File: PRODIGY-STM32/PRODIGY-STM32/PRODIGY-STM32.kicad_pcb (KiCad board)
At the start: 2 copper layers, 55 x 40 mm, 64 parts, among them J1 DF40C-100DP-04V-51, J2 DF40C-100DP-04V-51, Q1 BC850, U1 AP2112K-3.3, U2 STM32F103C8Tx, U3 STM32F407VGTx, Y1 8MHz, Y2 8MHz, Y3 32.768kHz

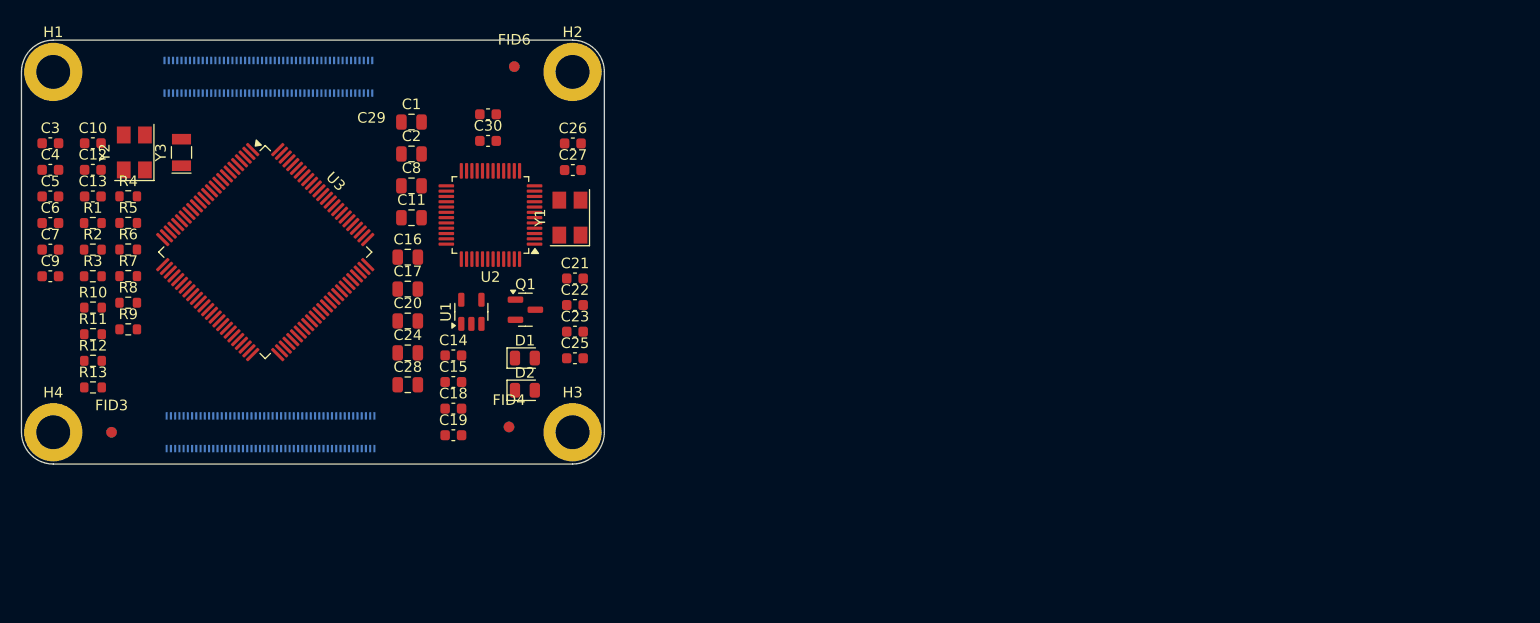
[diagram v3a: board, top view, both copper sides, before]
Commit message: stm32 started, footprints updated, lazout started
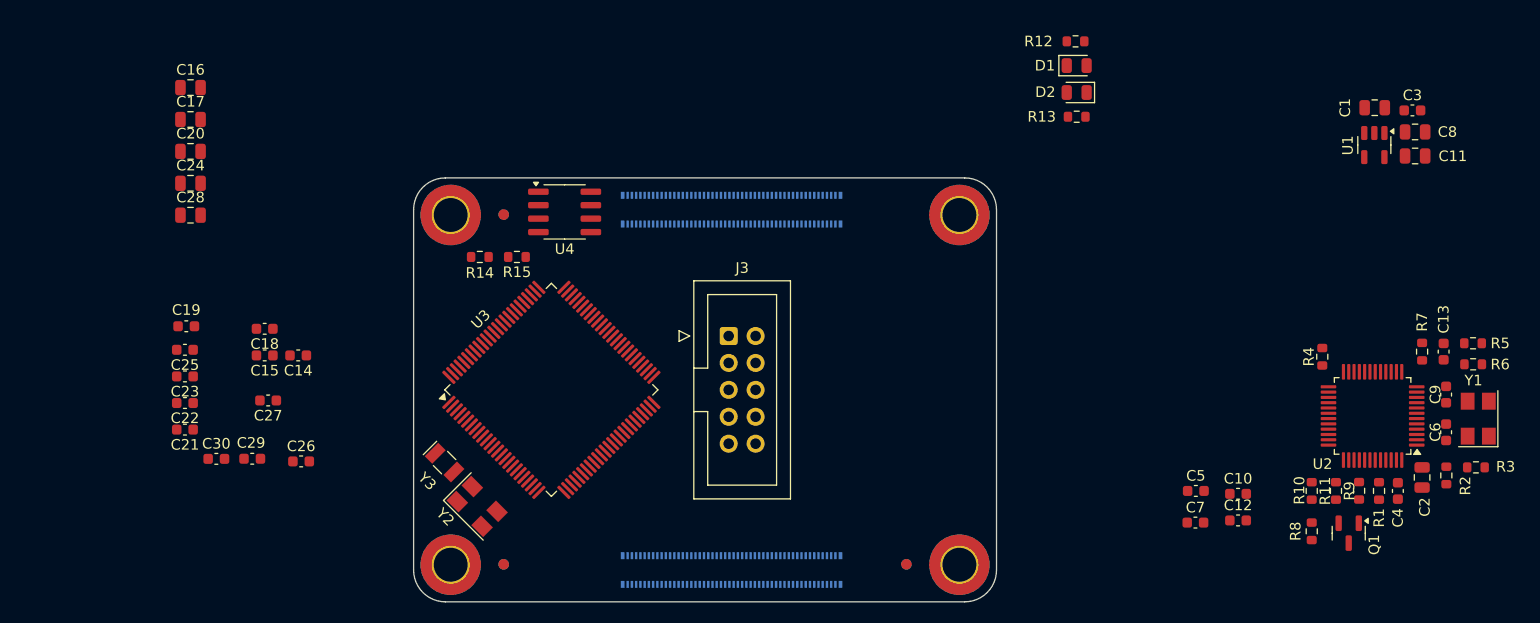
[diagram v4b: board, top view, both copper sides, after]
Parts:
- added J3: Conn_ARM_JTAG_SWD_10, Connector_IDC:IDC-Header_2x05_P2.54mm_Vertical, F.Cu at (166.7, 82.9)
- added R14: DNP, Resistor_SMD:R_0603_1608Metric, F.Cu at (143.2, 75.5)
- added R15: DNP, Resistor_SMD:R_0603_1608Metric, F.Cu at (146.8, 75.5)
- added U4: M24C32-WMN6TP, Package_SO:SOIC-8_3.9x4.9mm_P1.27mm, F.Cu at (151.2, 71.2)
- H1, H2, H3, H4: footprint MountingHole:MountingHole_3.2mm_M3_ISO14580_Pad -> MountingHole:MountingHole_3.2mm_M3_ISO7380_Pad_TopBottom
- J1, J2: footprint DF40C:HIROSE_DF40C-100DS-0.4V_51_ -> DF40C-100DP-0:DF40C100DP04V51
- moved C6 133.2 mm to (234.4, 92.0), turned to -90 degrees
- moved C9 132.2 mm to (234.4, 88.4), turned to 90 degrees
- moved R3 131.7 mm to (237.2, 95.3)
- moved C4 130.7 mm to (229.9, 97.5), turned to -90 degrees
- moved R2 129.5 mm to (234.4, 96.1), turned to -90 degrees
- moved C3 128.6 mm to (231.2, 61.6)
- moved C13 128.3 mm to (234.2, 84.4), turned to 90 degrees
- moved R5 127.4 mm to (237.0, 83.6), turned to 180 degrees
- moved R6 127.4 mm to (237.0, 85.6)
- moved R1 124.0 mm to (228.1, 97.5), turned to -90 degrees
- moved R7 122.3 mm to (232.2, 84.4), turned to -90 degrees
- moved R11 118.2 mm to (224.0, 97.5), turned to 90 degrees
- moved R9 117.1 mm to (226.2, 97.5), turned to -90 degrees
- moved R10 116.3 mm to (221.7, 97.5), turned to 90 degrees
- moved R8 113.7 mm to (221.7, 101.3), turned to -90 degrees
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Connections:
- net /mcu/T_DIO renamed /st-link-v2/T_DIO
- net /mcu/T_RST renamed /st-link-v2/T_RST
- net /mcu/T_SWO renamed /st-link-v2/T_SWO
- J1 pad 1: /Connector-1/USB_HOST_FAULT -> /Connector-1/ANALOG_MICROPHONE
- J1 pad 10: /Connector-1/SERIAL_OUT_TX2 -> GND
- J1 pad 100: /Connector-1/ANALOG_BREAKOUT_PIEZO -> /Connector-1/USB_HOST_ENABLE
- J1 pad 11: /Connector-1/SERIAL_OUT_TX1 -> unconnected-(J1-Pad11)
- J1 pad 12: /Connector-1/SERIAL_OUT_RX2 -> unconnected-(J1-Pad12)
- J1 pad 13: GND -> /Connector-1/ANALOG_JOYSTICK_X
- J1 pad 14: GND -> /Connector-1/ANALOG_HEATER_TEMPERATURE
- J1 pad 15: /Connector-1/CAN_OUT_TX1 -> GND
- J1 pad 16: /Connector-1/CAN_EN -> GND
- J1 pad 17: /Connector-1/CAN_OUT_RX1 -> unconnected-(J1-Pad17)
- J1 pad 18: /Connector-1/CAN_SILENT -> unconnected-(J1-Pad18)
- J1 pad 19: GND -> /Connector-1/ANALOG_PHOTOTRANSISTOR
- J1 pad 2: /Connector-1/USB_HOST_ENABLE -> /Connector-1/ANALOG_BREAKOUT_PIEZO
- J1 pad 20: GND -> /Connector-1/ANALOG_POTENTIOMETER
- J1 pad 21: /Connector-1/I2C_SDA -> GND
- J1 pad 22: /Connector-1/SPI_MOSI -> GND
- J1 pad 23: /Connector-1/I2C_SCL -> unconnected-(J1-Pad23)
- J1 pad 24: /Connector-1/SPI_MISO -> unconnected-(J1-Pad24)
- J1 pad 25: GND -> unconnected-(J1-Pad25)
- J1 pad 26: GND -> unconnected-(J1-Pad26)
- J1 pad 27: /Connector-1/I2C_INTERRUPT_ACCEL -> GND
- J1 pad 28: /Connector-1/SPI_SCK -> GND
- J1 pad 29: /Connector-1/I2C_INTERRUPT_KEYPAD -> unconnected-(J1-Pad29)
- J1 pad 3: /Connector-1/USB_DP- -> GND
- J1 pad 30: /Connector-1/SPI_CS_BREAKOUT -> unconnected-(J1-Pad30)
- J1 pad 31: GND -> unconnected-(J1-Pad31)
- J1 pad 32: GND -> unconnected-(J1-Pad32)
- J1 pad 33: /Connector-1/DIGITAL_IR_EMITTER -> GND
- J1 pad 34: /Connector-1/SPI_CS_SEVENSEG -> GND
- J1 pad 35: /Connector-1/DIGITAL_IR_RECEIVER -> /Connector-1/MOTOR_CC_IN_1
- J1 pad 36: /Connector-1/SPI_CS_TFT -> /Connector-1/MOTOR_CC_IN_2
- J1 pad 37: GND -> /Connector-1/MOTOR_PWM_OUT_1
- J1 pad 38: GND -> /Connector-1/MOTOR_PWM_OUT_2
- J1 pad 39: /Connector-1/DIGITAL_NEOPIXEL_OUT -> GND
- J1 pad 4: /Connector-1/USB_HOST_OUT_P- -> GND
- J1 pad 40: /Connector-1/SPI_TFT_DC -> GND
- J1 pad 41: /Connector-1/DIGITAL_RGB_R -> /Connector-1/DIGITAL_LED_OUT_1
- J1 pad 42: /Connector-1/SPI_TFT_RESET -> /Connector-1/DIGITAL_BUZZER_OUT
- J1 pad 43: /Connector-1/DIGITAL_RGB_G -> /Connector-1/DIGITAL_LED_OUT_0
- J1 pad 44: GND -> /Connector-1/DIGITAL_LED_OUT_2
- J1 pad 45: /Connector-1/DIGITAL_RGB_B -> GND
- J1 pad 46: /Connector-1/SPI_CS_NFC -> GND
- J1 pad 47: /Connector-1/DIGITAL_BUTTON_IN_0 -> /Connector-1/DIGITAL_BUTTON_IN_3
- J1 pad 48: /Connector-1/SPI_IRQ_NFC -> /Connector-1/DIGITAL_HEATER_OUT
- J1 pad 49: /Connector-1/DIGITAL_BUTTON_IN_1 -> /Connector-1/DIGITAL_BUTTON_IN_2
- J1 pad 5: /st-link-v2/USB_D+ -> unconnected-(J1-Pad5)
- J1 pad 50: GND -> /Connector-1/SPI_RST_NFC
- J1 pad 51: /Connector-1/DIGITAL_BUTTON_IN_2 -> /Connector-1/DIGITAL_BUTTON_IN_1
- J1 pad 52: /Connector-1/SPI_RST_NFC -> GND
- J1 pad 53: /Connector-1/DIGITAL_BUTTON_IN_3 -> /Connector-1/DIGITAL_BUTTON_IN_0
- J1 pad 54: /Connector-1/DIGITAL_HEATER_OUT -> /Connector-1/SPI_IRQ_NFC
- J1 pad 55: GND -> /Connector-1/DIGITAL_RGB_B
- J1 pad 56: GND -> /Connector-1/SPI_CS_NFC
- J1 pad 57: /Connector-1/DIGITAL_LED_OUT_0 -> /Connector-1/DIGITAL_RGB_G
- J1 pad 58: /Connector-1/DIGITAL_LED_OUT_2 -> GND
- J1 pad 59: /Connector-1/DIGITAL_LED_OUT_1 -> /Connector-1/DIGITAL_RGB_R
- J1 pad 6: /Connector-1/USB_HOST_OUT_P+ -> unconnected-(J1-Pad6)
- J1 pad 60: /Connector-1/DIGITAL_BUZZER_OUT -> /Connector-1/SPI_TFT_RESET
- J1 pad 61: GND -> /Connector-1/DIGITAL_NEOPIXEL_OUT
- J1 pad 62: GND -> /Connector-1/SPI_TFT_DC
- J1 pad 63: /Connector-1/MOTOR_PWM_OUT_1 -> GND
- J1 pad 64: /Connector-1/MOTOR_PWM_OUT_2 -> GND
- J1 pad 65: /Connector-1/MOTOR_CC_IN_1 -> /Connector-1/DIGITAL_IR_RECEIVER
- J1 pad 66: /Connector-1/MOTOR_CC_IN_2 -> /Connector-1/SPI_CS_TFT
- J1 pad 67: GND -> /Connector-1/DIGITAL_IR_EMITTER
- J1 pad 68: GND -> /Connector-1/SPI_CS_SEVENSEG
- J1 pad 69: unconnected-(J1-Pad69) -> GND
- J1 pad 7: GND -> /Connector-1/ANALOG_JOYSTICK_Y
- J1 pad 70: unconnected-(J1-Pad70) -> GND
- J1 pad 71: unconnected-(J1-Pad71) -> /Connector-1/I2C_INTERRUPT_KEYPAD
- J1 pad 72: unconnected-(J1-Pad72) -> /Connector-1/SPI_CS_BREAKOUT
- J1 pad 73: GND -> /Connector-1/I2C_INTERRUPT_ACCEL
- J1 pad 74: GND -> /Connector-1/SPI_SCK
- J1 pad 75: unconnected-(J1-Pad75) -> GND
- J1 pad 76: unconnected-(J1-Pad76) -> GND
- J1 pad 77: unconnected-(J1-Pad77) -> /mcu/SCL
- J1 pad 78: unconnected-(J1-Pad78) -> /Connector-1/SPI_MISO
- J1 pad 79: GND -> /mcu/SDA
- J1 pad 8: GND -> /Connector-1/ANALOG_BREAKOUT_PT100
- J1 pad 80: GND -> /Connector-1/SPI_MOSI
- J1 pad 81: /Connector-1/ANALOG_PHOTOTRANSISTOR -> GND
- J1 pad 82: /Connector-1/ANALOG_POTENTIOMETER -> GND
- J1 pad 83: unconnected-(J1-Pad83) -> /Connector-1/CAN_OUT_RX1
- J1 pad 84: unconnected-(J1-Pad84) -> /Connector-1/CAN_SILENT
- J1 pad 85: GND -> /Connector-1/CAN_OUT_TX1
- J1 pad 86: GND -> /Connector-1/CAN_EN
- J1 pad 87: /Connector-1/ANALOG_JOYSTICK_X -> GND
- J1 pad 88: /Connector-1/ANALOG_HEATER_TEMPERATURE -> GND
- J1 pad 89: unconnected-(J1-Pad89) -> /Connector-1/SERIAL_OUT_TX1
- J1 pad 9: /Connector-1/SERIAL_OUT_RX1 -> GND
- J1 pad 90: unconnected-(J1-Pad90) -> /Connector-1/SERIAL_OUT_RX2
- J1 pad 91: GND -> /Connector-1/SERIAL_OUT_RX1
- J1 pad 92: GND -> /Connector-1/SERIAL_OUT_TX2
- J1 pad 93: /Connector-1/ANALOG_JOYSTICK_Y -> GND
- J1 pad 94: /Connector-1/ANALOG_BREAKOUT_PT100 -> GND
- J1 pad 95: unconnected-(J1-Pad95) -> /st-link-v2/USB_D+
- J1 pad 96: unconnected-(J1-Pad96) -> /Connector-1/USB_HOST_OUT_P+
- J1 pad 97: GND -> /Connector-1/USB_DP-
- J1 pad 98: GND -> /Connector-1/USB_HOST_OUT_P-
- J1 pad 99: /Connector-1/ANALOG_MICROPHONE -> /Connector-1/USB_HOST_FAULT
- J2 pad 1: GND -> unconnected-(J2-Pad1)
- J2 pad 100: /Connector-2/MCU_RESET -> GND
- J2 pad 12: unconnected-(J2-Pad12) -> +3V3
- J2 pad 13: GND -> +5V
- J2 pad 14: GND -> +3V3
- J2 pad 15: unconnected-(J2-Pad15) -> +5V
- J2 pad 16: unconnected-(J2-Pad16) -> +3V3
- J2 pad 17: unconnected-(J2-Pad17) -> +5V
- J2 pad 18: unconnected-(J2-Pad18) -> +3V3
- J2 pad 19: unconnected-(J2-Pad19) -> +5V
- J2 pad 2: GND -> /Connector-2/MCU_RESET
- J2 pad 21: unconnected-(J2-Pad21) -> +5V
- J2 pad 22: GND -> unconnected-(J2-Pad22)
- J2 pad 23: GND -> +5V
- J2 pad 24: /Connector-2/MCU_GPIO_26 -> /Connector-2/MCU_VREF
- J2 pad 25: /Connector-2/MCU_GPIO_21 -> /Connector-2/SD_Enable
- J2 pad 26: /Connector-2/MCU_GPIO_19 -> /Connector-2/SD_DET
- J2 pad 27: /Connector-2/MCU_GPIO_20 -> unconnected-(J2-Pad27)
- J2 pad 28: /Connector-2/MCU_GPIO_13 -> GND
- J2 pad 29: /Connector-2/MCU_GPIO_16 -> GND
- J2 pad 30: /Connector-2/MCU_GPIO_6 -> unconnected-(J2-Pad30)
- J2 pad 31: /Connector-2/MCU_GPIO_12 -> /Connector-2/SD_DAT2
- J2 pad 32: GND -> unconnected-(J2-Pad32)
- J2 pad 33: GND -> /Connector-2/SD_DAT1
- J2 pad 34: /Connector-2/MCU_GPIO_5 -> unconnected-(J2-Pad34)
- J2 pad 35: unconnected-(J2-Pad35) -> GND
- J2 pad 36: unconnected-(J2-Pad36) -> GND
- J2 pad 37: /Connector-2/MCU_GPIO_7 -> /Connector-2/SD_DAT0
- J2 pad 38: /Connector-2/MCU_GPIO_11 -> unconnected-(J2-Pad38)
- J2 pad 39: /Connector-2/MCU_GPIO_8 -> /Connector-2/SD_DAT3
- J2 pad 4: unconnected-(J2-Pad4) -> GND
- J2 pad 40: /Connector-2/MCU_GPIO_9 -> /Connector-2/SD_CMD
- J2 pad 41: /Connector-2/MCU_GPIO_25 -> GND
- J2 pad 43: GND -> /Connector-2/SD_CLK
- J2 pad 44: /Connector-2/MCU_GPIO_10 -> /Connector-2/MCU_GPIO_2
- J2 pad 45: /Connector-2/MCU_GPIO_24 -> /Connector-2/MCU_GPIO_14
- J2 pad 46: /Connector-2/MCU_GPIO_22 -> /Connector-2/MCU_GPIO_3
- J2 pad 47: /Connector-2/MCU_GPIO_23 -> GND
- J2 pad 48: /Connector-2/MCU_GPIO_27 -> /Connector-2/MCU_GPIO_4
- J2 pad 49: /Connector-2/MCU_GPIO_18 -> /Connector-2/MCU_GPIO_15
- J2 pad 50: /Connector-2/MCU_GPIO_17 -> GND
- J2 pad 51: /Connector-2/MCU_GPIO_15 -> /Connector-2/MCU_GPIO_18
- J2 pad 52: GND -> /Connector-2/MCU_GPIO_17
- J2 pad 53: GND -> /Connector-2/MCU_GPIO_23
- J2 pad 54: /Connector-2/MCU_GPIO_4 -> /Connector-2/MCU_GPIO_27
- J2 pad 55: /Connector-2/MCU_GPIO_14 -> /Connector-2/MCU_GPIO_24
- J2 pad 56: /Connector-2/MCU_GPIO_3 -> /Connector-2/MCU_GPIO_22
- J2 pad 57: /Connector-2/SD_CLK -> GND
- J2 pad 58: /Connector-2/MCU_GPIO_2 -> /Connector-2/MCU_GPIO_10
- J2 pad 59: GND -> /Connector-2/MCU_GPIO_25
- J2 pad 61: /Connector-2/SD_DAT3 -> /Connector-2/MCU_GPIO_8
- J2 pad 62: /Connector-2/SD_CMD -> /Connector-2/MCU_GPIO_9
- J2 pad 63: /Connector-2/SD_DAT0 -> /Connector-2/MCU_GPIO_7
- J2 pad 64: unconnected-(J2-Pad64) -> /Connector-2/MCU_GPIO_11
- J2 pad 65: GND -> unconnected-(J2-Pad65)
- J2 pad 66: GND -> unconnected-(J2-Pad66)
- J2 pad 67: /Connector-2/SD_DAT1 -> GND
- J2 pad 68: unconnected-(J2-Pad68) -> /Connector-2/MCU_GPIO_5
- J2 pad 69: /Connector-2/SD_DAT2 -> /Connector-2/MCU_GPIO_12
- J2 pad 7: GND -> unconnected-(J2-Pad7)
- J2 pad 70: unconnected-(J2-Pad70) -> GND
- J2 pad 71: GND -> /Connector-2/MCU_GPIO_16
- J2 pad 72: unconnected-(J2-Pad72) -> /Connector-2/MCU_GPIO_6
- J2 pad 73: unconnected-(J2-Pad73) -> /Connector-2/MCU_GPIO_20
- J2 pad 74: GND -> /Connector-2/MCU_GPIO_13
- J2 pad 75: /Connector-2/SD_Enable -> /Connector-2/MCU_GPIO_21
- J2 pad 76: /Connector-2/SD_DET -> /Connector-2/MCU_GPIO_19
- J2 pad 77: +5V -> GND
- J2 pad 78: /Connector-2/MCU_VREF -> /Connector-2/MCU_GPIO_26
- J2 pad 79: +5V -> unconnected-(J2-Pad79)
- J2 pad 8: GND -> unconnected-(J2-Pad8)
- J2 pad 80: unconnected-(J2-Pad80) -> GND
- J2 pad 81: +5V -> unconnected-(J2-Pad81)
- J2 pad 83: +5V -> unconnected-(J2-Pad83)
- J2 pad 84: +3V3 -> unconnected-(J2-Pad84)
- J2 pad 85: +5V -> unconnected-(J2-Pad85)
- J2 pad 86: +3V3 -> unconnected-(J2-Pad86)
- J2 pad 87: +5V -> GND
- J2 pad 88: +3V3 -> GND
- J2 pad 90: +3V3 -> unconnected-(J2-Pad90)
- J2 pad 93: unconnected-(J2-Pad93) -> GND
- J2 pad 94: unconnected-(J2-Pad94) -> GND
- J2 pad 98: GND -> unconnected-(J2-Pad98)
- J2 pad 99: unconnected-(J2-Pad99) -> GND
- U3 pad 92: /Connector-1/I2C_SCL -> /mcu/SCL
- U3 pad 93: /Connector-1/I2C_SDA -> /mcu/SDA
- Y1 pad 2: Net-(U2-PD1) -> GND
- Y1 pad 3: (no net) -> Net-(U2-PD1)
- Y1 pad 4: (no net) -> GND
- Y2 pad 2: Net-(U3-PH1) -> GND
- Y2 pad 3: (no net) -> Net-(U3-PH1)
- Y2 pad 4: (no net) -> GND
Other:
- copper layers 2 -> 4

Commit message: stm32 layout done, schematic swd coinnector updated
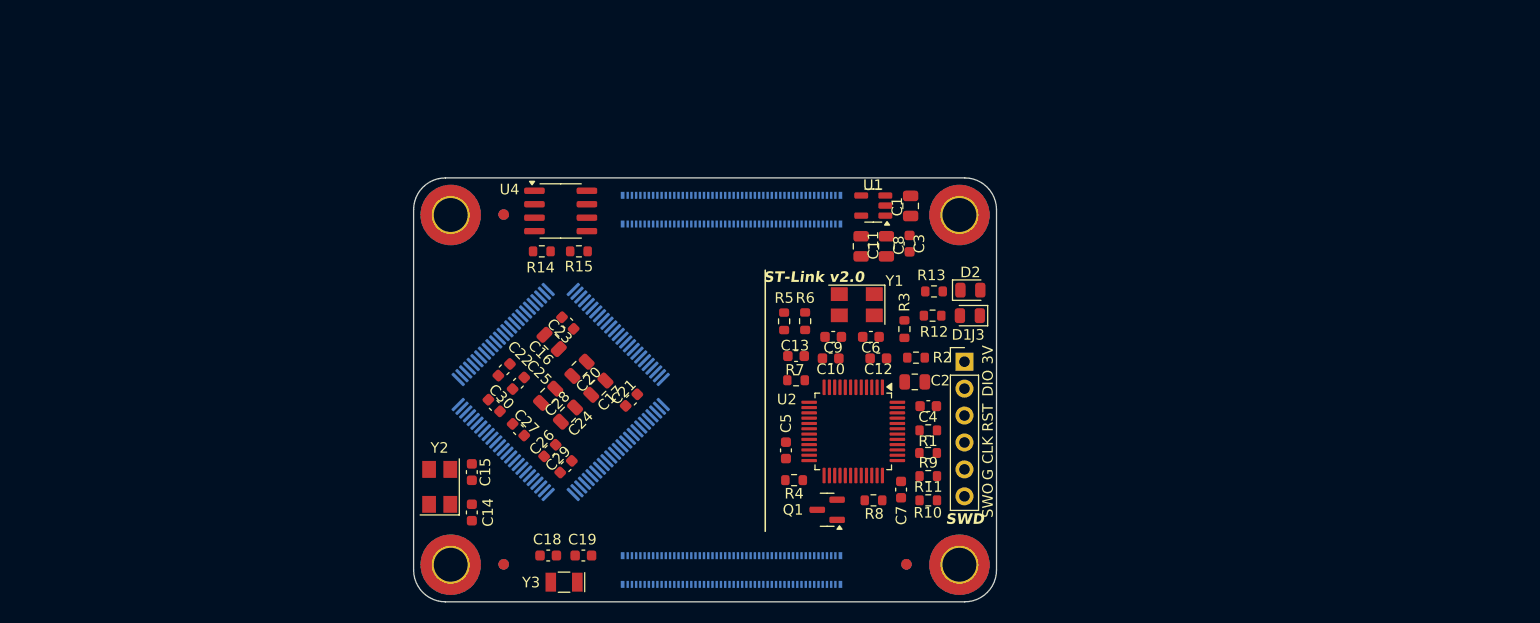
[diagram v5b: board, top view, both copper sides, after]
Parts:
- J3: value Conn_ARM_JTAG_SWD_10 -> Conn_ARM_SWD_TagConnect_TC2030; footprint Connector_IDC:IDC-Header_2x05_P2.54mm_Vertical -> Connector_PinHeader_2.54mm:PinHeader_1x06_P2.54mm_Vertical
- U3: moved to B.Cu
- moved R5 65.0 mm to (172.0, 81.5), turned to -90 degrees
- moved R6 63.2 mm to (173.9, 81.5), turned to 90 degrees
- moved C13 61.1 mm to (173.1, 84.8), turned to 180 degrees
- moved Y1 59.6 mm to (178.8, 80.0), turned to 180 degrees
- moved R7 59.1 mm to (173.1, 87.1), turned to 0 degrees
- moved C9 58.1 mm to (176.6, 83.0), turned to 180 degrees
- moved R3 55.5 mm to (183.3, 82.3), turned to 90 degrees
- moved C6 55.0 mm to (180.2, 83.0), turned to 0 degrees
- moved C11 53.0 mm to (179.2, 74.5), turned to -90 degrees
- moved R2 51.3 mm to (184.4, 85.0), turned to 0 degrees
- moved R4 51.2 mm to (172.9, 96.5), turned to 0 degrees
- moved C8 51.0 mm to (181.6, 74.5), turned to -90 degrees
- moved Q1 49.3 mm to (176.0, 99.3), turned to 180 degrees
- moved C3 49.1 mm to (183.8, 74.2), turned to -90 degrees
- moved U2 49.0 mm to (178.5, 91.9), turned to -90 degrees
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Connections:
- J3 pad 3: GND -> /st-link-v2/T_RST
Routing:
- added copper zone on In2.Cu, net GND
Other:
- board text added: "3V"
- board text added: "CLK"
- board text added: "DIO"
- board text added: "G"
- board text added: "RST"
- board text added: "ST-Link v2.0"
- board text added: "SWD"
- board text added: "SWO"

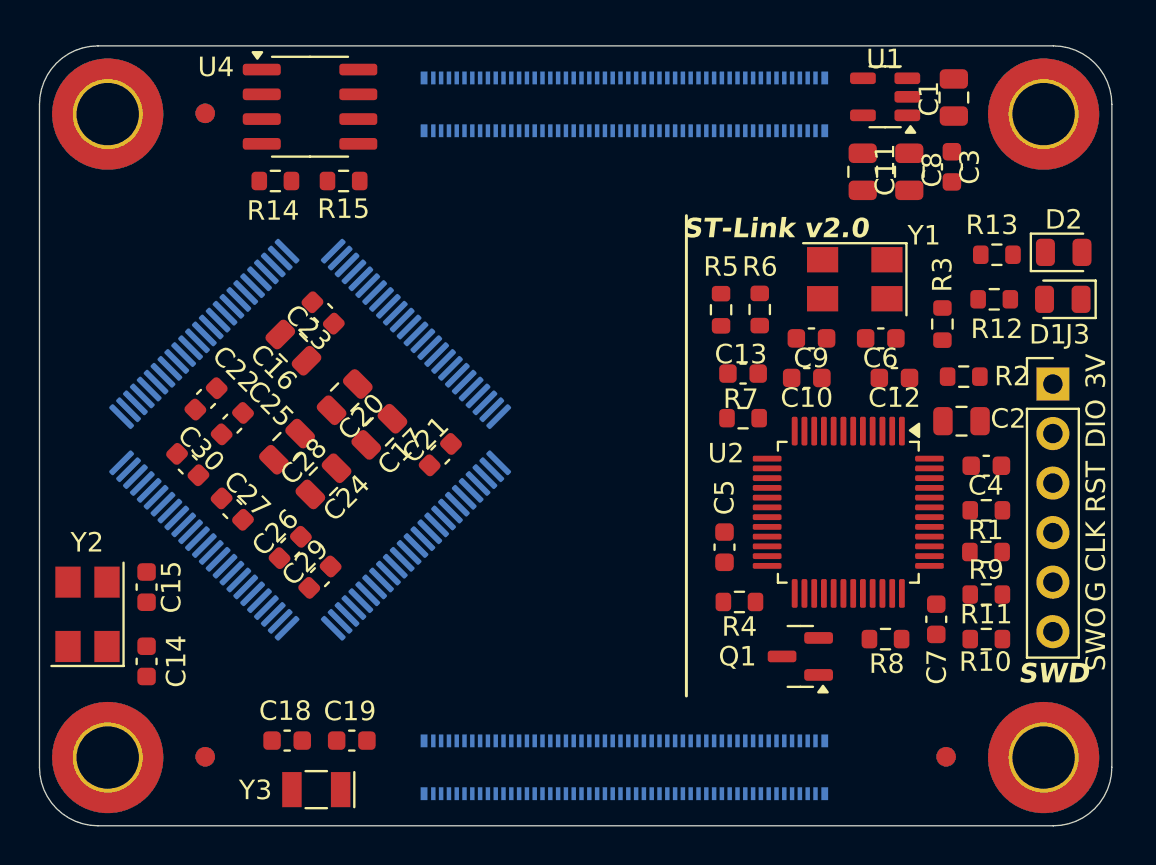
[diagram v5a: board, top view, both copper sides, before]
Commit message: stlink wiring done, power vias placed, anlog routing almost done
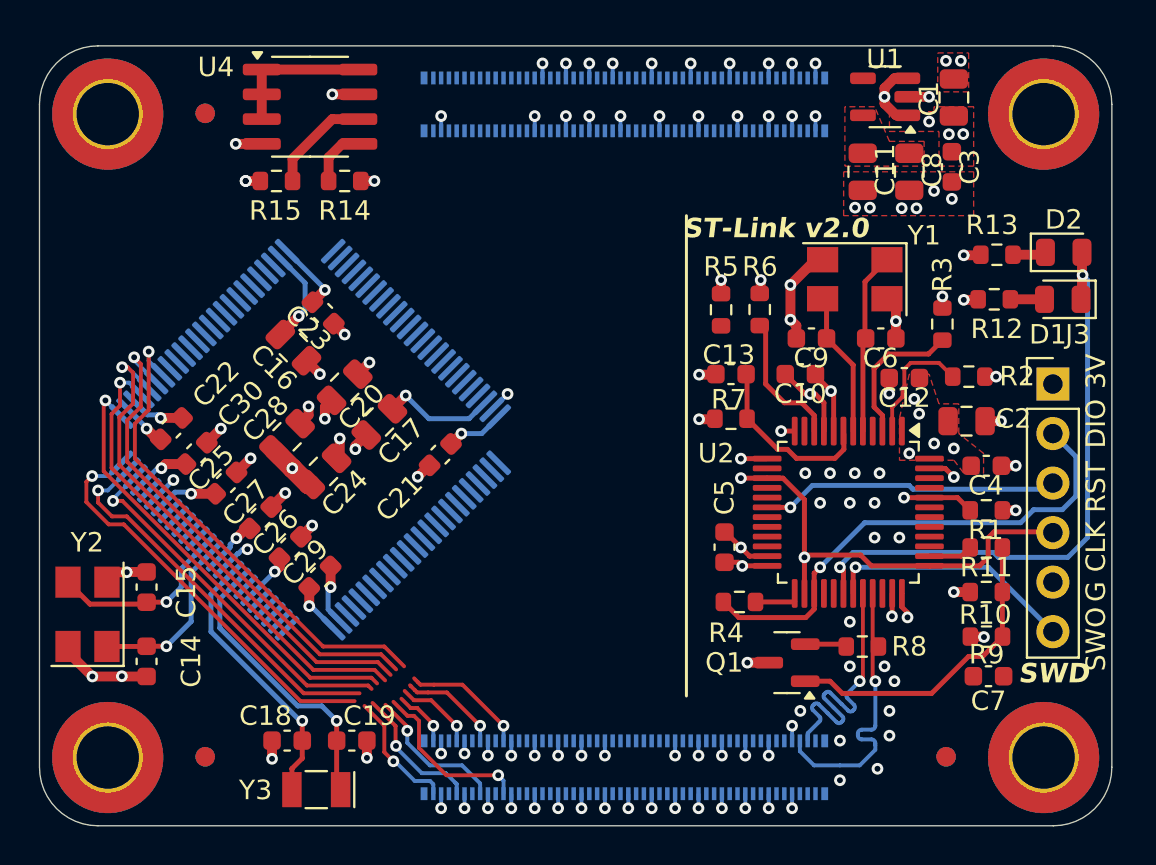
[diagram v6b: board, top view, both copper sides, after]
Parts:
- moved R9 4.34 mm to (185.6, 98.3)
- moved C7 3.96 mm to (185.7, 100.3), turned to 0 degrees
- moved R14 3.56 mm to (152.7, 74.9), turned to 180 degrees
- moved R15 3.44 mm to (149.2, 74.9), turned to 0 degrees
- moved R10 2.41 mm to (185.6, 96.0)
- moved R11 2.41 mm to (185.6, 93.7)
- moved C30 2.40 mm to (145.0, 88.9)
- moved C22 2.34 mm to (143.8, 87.6), turned to -135 degrees
- moved C25 2.17 mm to (146.6, 90.4), turned to 45 degrees
- moved C27 1.51 mm to (148.3, 92.2), turned to 45 degrees
- moved R8 1.25 mm to (179.2, 98.8), turned to 0 degrees
- moved Q1 0.75 mm to (175.3, 99.6)
- moved R7 0.62 mm to (172.5, 87.1)
- moved C13 0.62 mm to (172.5, 84.8)
- moved C24 0.51 mm to (151.6, 89.8)
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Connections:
- C10 pad 1: +3V3 -> /st-link-v2/+3V3_STLINK
- C11 pad 1: +3V3 -> /st-link-v2/+3V3_STLINK
- C12 pad 1: +3V3 -> /st-link-v2/+3V3_STLINK
- C2 pad 1: +3V3 -> /st-link-v2/+3V3_STLINK
- C4 pad 1: +3V3 -> /st-link-v2/+3V3_STLINK
- C5 pad 1: +3V3 -> /st-link-v2/+3V3_STLINK
- C7 pad 1: +3V3 -> /st-link-v2/+3V3_STLINK
- C8 pad 1: +3V3 -> /st-link-v2/+3V3_STLINK
- J3 pad 1: +3V3 -> /st-link-v2/+3V3_STLINK
- Q1 pad 3: +3V3 -> /st-link-v2/+3V3_STLINK
- R12 pad 1: +3V3 -> /st-link-v2/+3V3_STLINK
- R5 pad 1: +3V3 -> /st-link-v2/+3V3_STLINK
- R7 pad 1: +3V3 -> /st-link-v2/+3V3_STLINK
- R9 pad 1: +3V3 -> /st-link-v2/+3V3_STLINK
- U1 pad 5: +3V3 -> /st-link-v2/+3V3_STLINK
- U2 pad 1: +3V3 -> /st-link-v2/+3V3_STLINK
- U2 pad 24: +3V3 -> /st-link-v2/+3V3_STLINK
- U2 pad 36: +3V3 -> /st-link-v2/+3V3_STLINK
- U2 pad 48: +3V3 -> /st-link-v2/+3V3_STLINK
- U2 pad 9: +3V3 -> /st-link-v2/+3V3_STLINK
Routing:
- net GND: track 0.00 -> 94.2 mm, vias 0 -> 119
- net +3V3: track 0.00 -> 34.8 mm, vias 0 -> 13
- net /Connector-1/ANALOG_HEATER_TEMPERATURE: track 0.00 -> 33.5 mm, vias 0 -> 2
- net /Connector-1/ANALOG_BREAKOUT_PT100: track 0.00 -> 32.7 mm, vias 0 -> 2
- net /Connector-1/ANALOG_BREAKOUT_PIEZO: track 0.00 -> 32.2 mm, vias 0 -> 2
- net /st-link-v2/LED: track 0.00 -> 30.9 mm, vias 0 -> 2
- net /Connector-1/ANALOG_POTENTIOMETER: track 0.00 -> 27.8 mm, vias 0 -> 2
- net /Connector-1/ANALOG_MICROPHONE: track 0.00 -> 27.6 mm, vias 0 -> 2
- net /Connector-1/ANALOG_JOYSTICK_Y: track 0.00 -> 27.6 mm, vias 0 -> 2
- net /Connector-1/ANALOG_JOYSTICK_X: track 0.00 -> 26.5 mm, vias 0 -> 2
- net /Connector-1/ANALOG_PHOTOTRANSISTOR: track 0.00 -> 26.5 mm, vias 0 -> 2
- net /st-link-v2/T_DIO: track 0.00 -> 25.8 mm, vias 0 -> 1
- net /st-link-v2/CLK: track 0.00 -> 22.9 mm, vias 0 -> 2
- net Net-(Q1-B): track 0.00 -> 16.2 mm
- net /st-link-v2/T_RST: track 0.00 -> 15.3 mm, vias 0 -> 1
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- added copper zone on F.Cu, net +5V
- added copper zone on F.Cu, net /st-link-v2/+3V3_STLINK
- added copper zone on In1.Cu, net /st-link-v2/+3V3_STLINK
- added copper zone on F.Cu, net GND
